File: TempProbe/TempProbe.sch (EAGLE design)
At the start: 15 parts, among them U2 ATTINY841

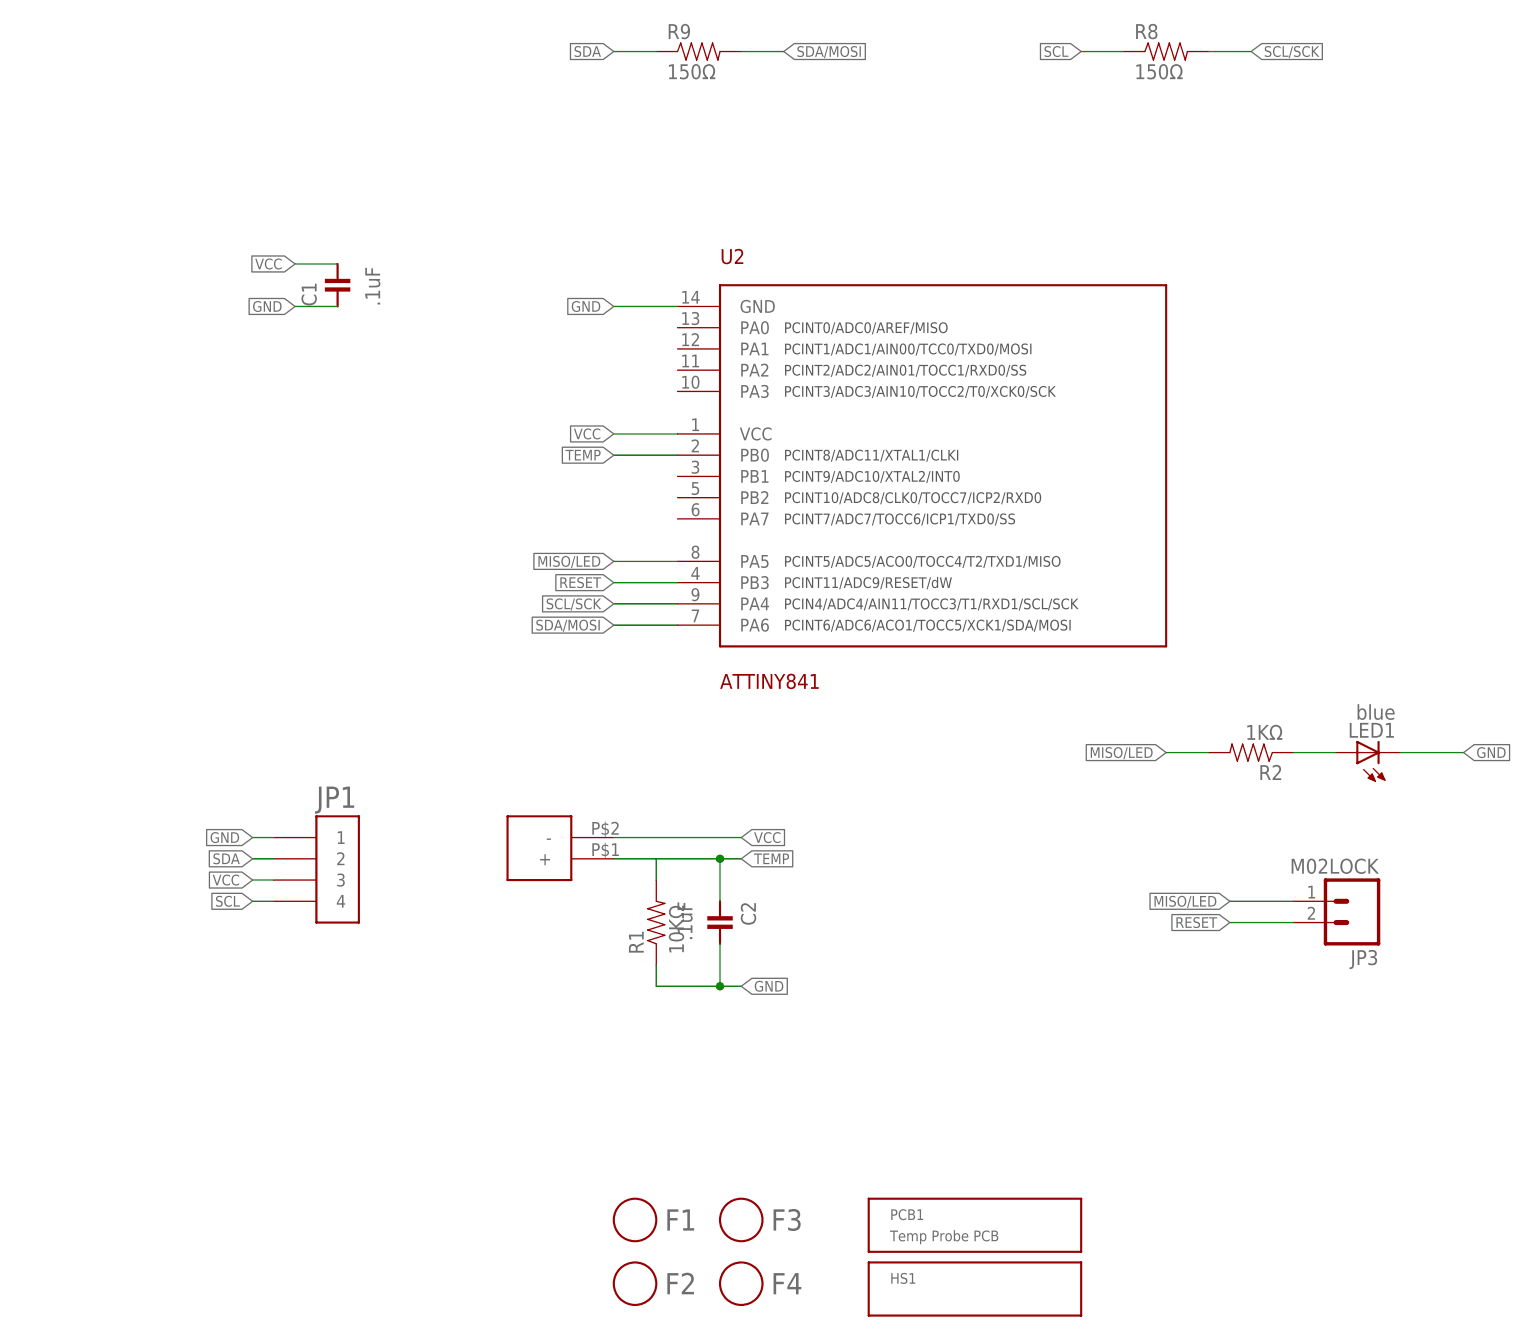
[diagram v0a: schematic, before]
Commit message: Changed to use Grove connector
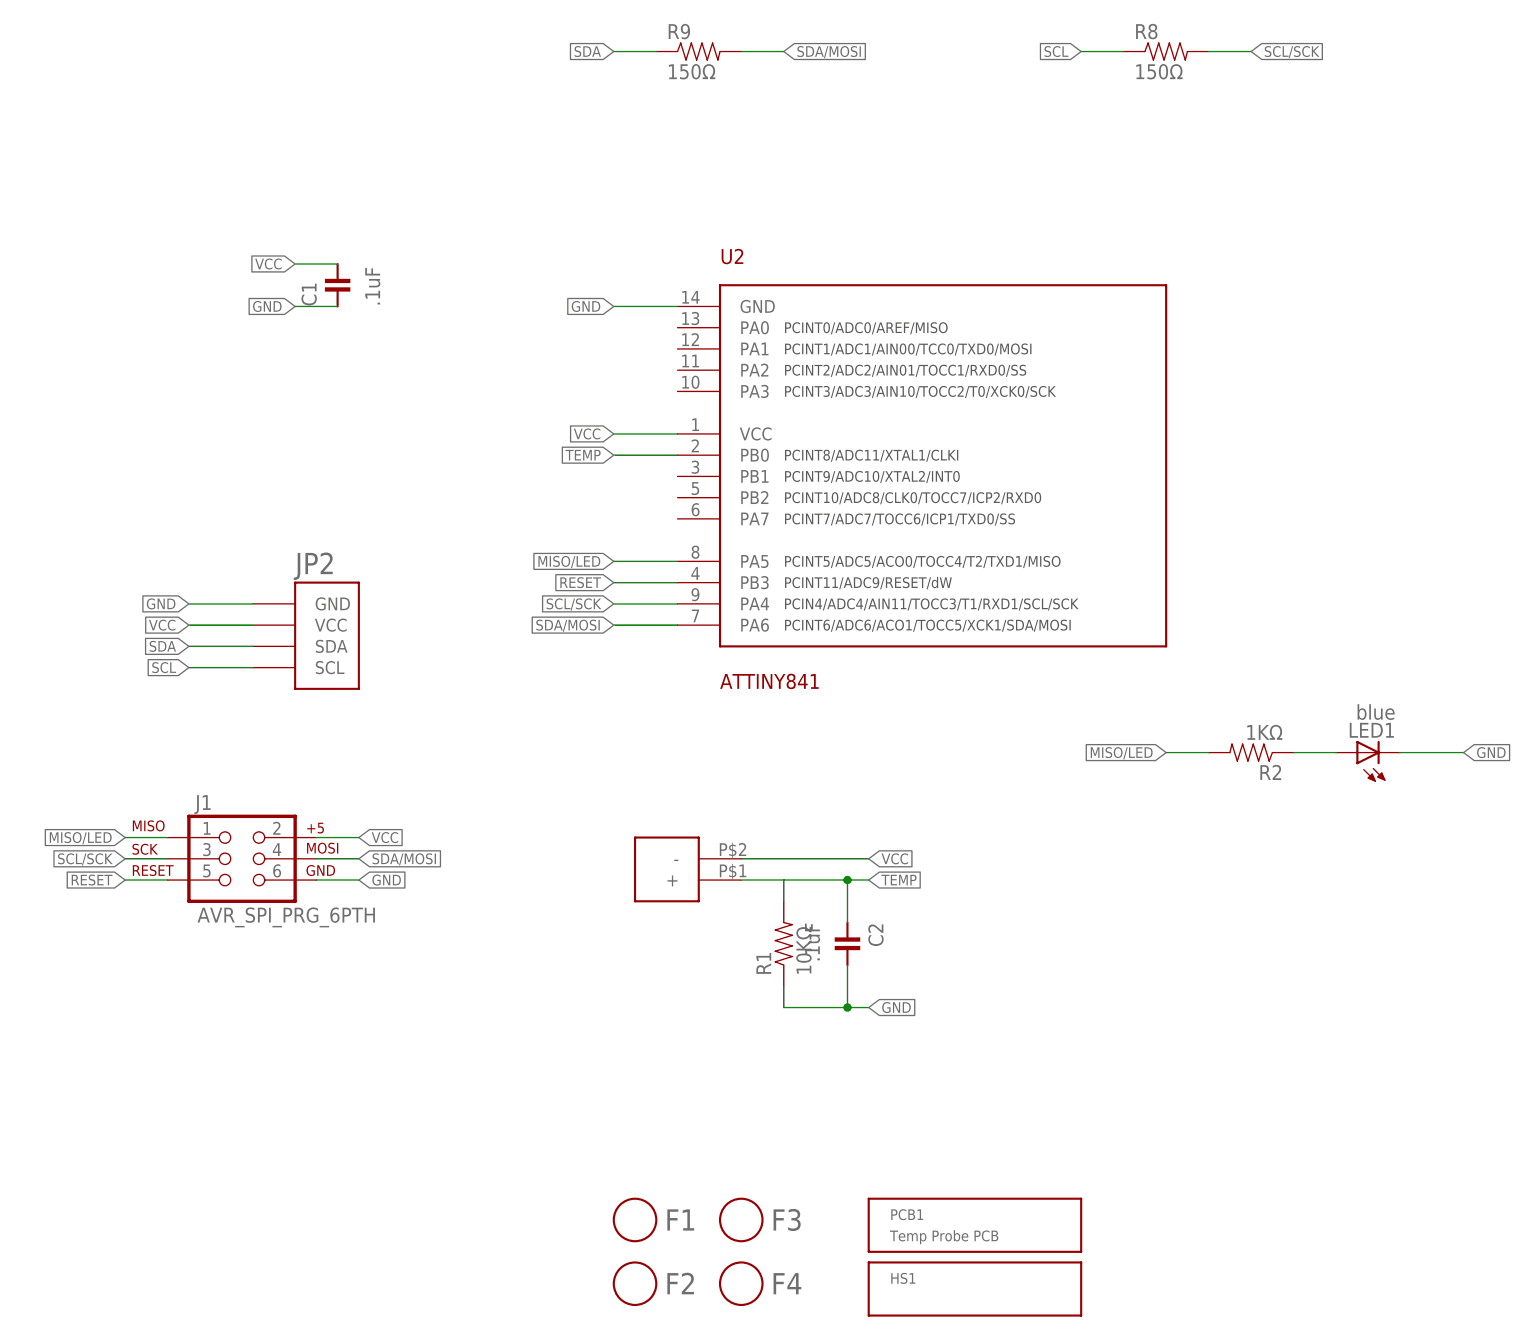
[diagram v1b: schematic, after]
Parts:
- removed JP1: HEADER-1X4-JST-PA-SIDE-SMD, Modulo:HEADER-1X4-JST-PA-SIDE-SMD
- removed JP3: M02LOCK, SparkFun-Connectors:M02LOCK
- added J1: AVR_SPI_PRG_6PTH, SparkFun-Connectors:AVR_SPI_PRG_6PTH
- added JP2: HEADER-MODULO, Modulo:HEADER-MODULO
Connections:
- net GND: now also J1.6, JP2.GND; no longer JP1.1
- net MISO/LED: now also J1.1; no longer JP3.1
- net RESET: now also J1.5; no longer JP3.2
- net SCL: now also JP2.SCL; no longer JP1.4
- net SCL/SCK: now also J1.3
- net SDA: now also JP2.SDA; no longer JP1.2
- net SDA/MOSI: now also J1.4
- net VCC: now also J1.2, JP2.VCC; no longer JP1.3
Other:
- moved on the sheet: C2, R1
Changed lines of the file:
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@@
 <part name="LED1" library="Modulo" deviceset="LED" device="-0805-BLUE" value="blue"/>
 <part name="R2" library="Modulo" deviceset="RESISTOR" device="-1KΩ" value="1KΩ"/>
-<part name="JP3" library="SparkFun-Connectors" deviceset="M02" device="LOCK">
-<attribute name="PARTNUM" value="EXCLUDE"/>
-</part>
 <part name="FRAME1" library="frames" deviceset="LETTER_L" device="">
 <attribute name="BOM" value="EXCLUDE"/>
@@
 <attribute name="PARTNUM" value="F221B1/2 CL210"/>
 </part>
-<part name="JP1" library="Modulo" deviceset="HEADER-1X4" device="-JST-PA-SIDE-SMD" value="HEADER-1X4-JST-PA-SIDE-SMD"/>
 <part name="U2" library="Modulo" deviceset="ATTINY841" device="" value="ATTINY841"/>
 <part name="R8" library="Modulo" deviceset="RESISTOR" device="-150Ω" value="150Ω">
@@
 <attribute name="PARTNUM" value="NTCLE413E2103F102L"/>
 </part>
+<part name="JP2" library="Modulo" deviceset="HEADER-MODULO" device=""/>
+<part name="J1" library="SparkFun-Connectors" deviceset="AVR_SPI_PRG_6" device="PTH"/>
 </parts>
 <sheets>
@@
 </plain>
 <instances>
-<instance part="C2" gate="G$1" x="93.98" y="68.58" rot="R180"/>
-<instance part="R1" gate="G$1" x="86.36" y="68.58" rot="R90"/>
+<instance part="C2" gate="G$1" x="109.22" y="66.04" rot="R180"/>
+<instance part="R1" gate="G$1" x="101.6" y="66.04" rot="R90"/>
 <instance part="C1" gate="G$1" x="48.26" y="144.78"/>
 <instance part="LED1" gate="G$1" x="170.18" y="88.9" rot="R90"/>
 <instance part="R2" gate="G$1" x="157.48" y="88.9" rot="R180"/>
-<instance part="JP3" gate="G$1" x="170.18" y="71.12" rot="R180">
-<attribute name="PARTNUM" x="170.18" y="71.12" size="1.27" layer="96" rot="R180" display="off"/>
-</instance>
 <instance part="FRAME1" gate="G$1" x="0" y="0">
 <attribute name="BOM" x="0" y="0" size="1.27" layer="96" display="off"/>
@@
 <attribute name="PARTNUM" x="116.84" y="22.86" size="1.27" layer="96" display="off"/>
 </instance>
-<instance part="JP1" gate="G$1" x="45.72" y="76.2"/>
 <instance part="U2" gate="G$1" x="99.06" y="114.3"/>
 <instance part="R8" gate="G$1" x="147.32" y="172.72">
@@
 <instance part="F3" gate="G$1" x="96.52" y="33.02"/>
 <instance part="F4" gate="G$1" x="96.52" y="25.4"/>
-<instance part="PROBE1" gate="G$1" x="73.66" y="76.2" rot="R180">
-<attribute name="PARTNUM" x="73.66" y="76.2" size="1.778" layer="96" rot="R180" display="off"/>
-</instance>
+<instance part="PROBE1" gate="G$1" x="88.9" y="73.66" rot="R180">
+<attribute name="PARTNUM" x="88.9" y="73.66" size="1.778" layer="96" rot="R180" display="off"/>
+</instance>
+<instance part="JP2" gate="G$1" x="45.72" y="101.6"/>
+<instance part="J1" gate="G$1" x="35.56" y="76.2"/>
 </instances>
 <busses>
@@
 <segment>
 <pinref part="R1" gate="G$1" pin="1"/>
-<wire x1="86.36" y1="63.5" x2="86.36" y2="60.96" width="0.1524" layer="91"/>
+<wire x1="101.6" y1="60.96" x2="101.6" y2="58.42" width="0.1524" layer="91"/>
 <pinref part="C2" gate="G$1" pin="1"/>
-<wire x1="93.98" y1="66.04" x2="93.98" y2="60.96" width="0.1524" layer="91"/>
-<wire x1="93.98" y1="60.96" x2="86.36" y2="60.96" width="0.1524" layer="91"/>
-<wire x1="93.98" y1="60.96" x2="96.52" y2="60.96" width="0.1524" layer="91"/>
-<label x="96.52" y="60.96" size="1.27" layer="95" xref="yes"/>
-<junction x="93.98" y="60.96"/>
+<wire x1="109.22" y1="63.5" x2="109.22" y2="58.42" width="0.1524" layer="91"/>
+<wire x1="109.22" y1="58.42" x2="101.6" y2="58.42" width="0.1524" layer="91"/>
+<wire x1="109.22" y1="58.42" x2="111.76" y2="58.42" width="0.1524" layer="91"/>
+<label x="111.76" y="58.42" size="1.27" layer="95" xref="yes"/>
+<junction x="109.22" y="58.42"/>
 </segment>
 <segment>
@@
 </segment>
 <segment>
-<pinref part="JP1" gate="G$1" pin="1"/>
-<wire x1="40.64" y1="78.74" x2="38.1" y2="78.74" width="0.1524" layer="91"/>
-<label x="38.1" y="78.74" size="1.27" layer="95" rot="R180" xref="yes"/>
-</segment>
-<segment>
 <pinref part="U2" gate="G$1" pin="GND"/>
 <wire x1="88.9" y1="142.24" x2="81.28" y2="142.24" width="0.1524" layer="91"/>
 <label x="81.28" y="142.24" size="1.27" layer="95" rot="MR0" xref="yes"/>
 </segment>
+<segment>
+<pinref part="JP2" gate="G$1" pin="GND"/>
+<wire x1="38.1" y1="106.68" x2="30.48" y2="106.68" width="0.1524" layer="91"/>
+<label x="30.48" y="106.68" size="1.27" layer="95" rot="R180" xref="yes"/>
+</segment>
+<segment>
+<pinref part="J1" gate="G$1" pin="6"/>
+<wire x1="45.72" y1="73.66" x2="50.8" y2="73.66" width="0.1524" layer="91"/>
+<label x="50.8" y="73.66" size="1.27" layer="95" xref="yes"/>
+</segment>
 </net>
 <net name="TEMP" class="0">
 <segment>
 <pinref part="R1" gate="G$1" pin="2"/>
-<wire x1="93.98" y1="76.2" x2="86.36" y2="76.2" width="0.1524" layer="91"/>
-<wire x1="86.36" y1="73.66" x2="86.36" y2="76.2" width="0.1524" layer="91"/>
+<wire x1="109.22" y1="73.66" x2="101.6" y2="73.66" width="0.1524" layer="91"/>
+<wire x1="101.6" y1="71.12" x2="101.6" y2="73.66" width="0.1524" layer="91"/>
 <pinref part="C2" gate="G$1" pin="2"/>
-<wire x1="93.98" y1="71.12" x2="93.98" y2="76.2" width="0.1524" layer="91"/>
-<wire x1="93.98" y1="76.2" x2="96.52" y2="76.2" width="0.1524" layer="91"/>
-<label x="96.52" y="76.2" size="1.27" layer="95" xref="yes"/>
-<junction x="93.98" y="76.2"/>
-<wire x1="81.28" y1="76.2" x2="86.36" y2="76.2" width="0.1524" layer="91"/>
+<wire x1="109.22" y1="68.58" x2="109.22" y2="73.66" width="0.1524" layer="91"/>
+<wire x1="109.22" y1="73.66" x2="111.76" y2="73.66" width="0.1524" layer="91"/>
+<label x="111.76" y="73.66" size="1.27" layer="95" xref="yes"/>
+<junction x="109.22" y="73.66"/>
+<wire x1="96.52" y1="73.66" x2="101.6" y2="73.66" width="0.1524" layer="91"/>
 <pinref part="PROBE1" gate="G$1" pin="+"/>
 </segment>
@@
 <net name="SDA" class="0">
 <segment>
-<pinref part="JP1" gate="G$1" pin="2"/>
-<wire x1="40.64" y1="76.2" x2="38.1" y2="76.2" width="0.1524" layer="91"/>
-<label x="38.1" y="76.2" size="1.27" layer="95" rot="R180" xref="yes"/>
-</segment>
-<segment>
 <pinref part="R9" gate="G$1" pin="1"/>
 <wire x1="86.36" y1="172.72" x2="81.28" y2="172.72" width="0.1524" layer="91"/>
 <label x="81.28" y="172.72" size="1.27" layer="95" rot="R180" xref="yes"/>
 </segment>
+<segment>
+<pinref part="JP2" gate="G$1" pin="SDA"/>
+<wire x1="38.1" y1="101.6" x2="30.48" y2="101.6" width="0.1524" layer="91"/>
+<label x="30.48" y="101.6" size="1.27" layer="95" rot="R180" xref="yes"/>
+</segment>
 </net>
 <net name="VCC" class="0">
@@
 </segment>
 <segment>
-<pinref part="JP1" gate="G$1" pin="3"/>
-<wire x1="40.64" y1="73.66" x2="38.1" y2="73.66" width="0.1524" layer="91"/>
-<label x="38.1" y="73.66" size="1.27" layer="95" rot="R180" xref="yes"/>
-</segment>
-<segment>
 <pinref part="U2" gate="G$1" pin="VCC"/>
 <wire x1="88.9" y1="127" x2="81.28" y2="127" width="0.1524" layer="91"/>
@@
 </segment>
 <segment>
-<wire x1="81.28" y1="78.74" x2="96.52" y2="78.74" width="0.1524" layer="91"/>
-<label x="96.52" y="78.74" size="1.27" layer="95" xref="yes"/>
+<wire x1="96.52" y1="76.2" x2="111.76" y2="76.2" width="0.1524" layer="91"/>
+<label x="111.76" y="76.2" size="1.27" layer="95" xref="yes"/>
 <pinref part="PROBE1" gate="G$1" pin="-"/>
 </segment>
+<segment>
+<pinref part="JP2" gate="G$1" pin="VCC"/>
+<wire x1="38.1" y1="104.14" x2="30.48" y2="104.14" width="0.1524" layer="91"/>
+<label x="30.48" y="104.14" size="1.27" layer="95" rot="R180" xref="yes"/>
+</segment>
+<segment>
+<pinref part="J1" gate="G$1" pin="2"/>
+<wire x1="45.72" y1="78.74" x2="50.8" y2="78.74" width="0.1524" layer="91"/>
+<label x="50.8" y="78.74" size="1.27" layer="95" xref="yes"/>
+</segment>
 </net>
 <net name="SCL" class="0">
-<segment>
-<pinref part="JP1" gate="G$1" pin="4"/>
-<wire x1="40.64" y1="71.12" x2="38.1" y2="71.12" width="0.1524" layer="91"/>
-<label x="38.1" y="71.12" size="1.27" layer="95" rot="R180" xref="yes"/>
-</segment>
 <segment>
 <pinref part="R8" gate="G$1" pin="1"/>
@@
 <label x="137.16" y="172.72" size="1.27" layer="95" rot="R180" xref="yes"/>
 </segment>
+<segment>
+<pinref part="JP2" gate="G$1" pin="SCL"/>
+<wire x1="38.1" y1="99.06" x2="30.48" y2="99.06" width="0.1524" layer="91"/>
+<label x="30.48" y="99.06" size="1.27" layer="95" rot="R180" xref="yes"/>
+</segment>
 </net>
 <net name="RESET" class="0">
@@
 </segment>
 <segment>
-<pinref part="JP3" gate="G$1" pin="2"/>
-<wire x1="162.56" y1="68.58" x2="154.94" y2="68.58" width="0.1524" layer="91"/>
-<label x="154.94" y="68.58" size="1.27" layer="95" rot="R180" xref="yes"/>
+<pinref part="J1" gate="G$1" pin="5"/>
+<wire x1="27.94" y1="73.66" x2="22.86" y2="73.66" width="0.1524" layer="91"/>
+<label x="22.86" y="73.66" size="1.27" layer="95" rot="R180" xref="yes"/>
 </segment>
 </net>
@@
 <label x="81.28" y="104.14" size="1.27" layer="95" rot="MR0" xref="yes"/>
 </segment>
+<segment>
+<pinref part="J1" gate="G$1" pin="4"/>
+<wire x1="45.72" y1="76.2" x2="50.8" y2="76.2" width="0.1524" layer="91"/>
+<label x="50.8" y="76.2" size="1.27" layer="95" xref="yes"/>
+</segment>
 </net>
 <net name="SCL/SCK" class="0">
@@
 <label x="81.28" y="106.68" size="1.27" layer="95" rot="MR0" xref="yes"/>
 </segment>
+<segment>
+<pinref part="J1" gate="G$1" pin="3"/>
+<wire x1="27.94" y1="76.2" x2="22.86" y2="76.2" width="0.1524" layer="91"/>
+<label x="22.86" y="76.2" size="1.27" layer="95" rot="R180" xref="yes"/>
+</segment>
 </net>
 <net name="MISO/LED" class="0">
@@
 </segment>
 <segment>
-<pinref part="JP3" gate="G$1" pin="1"/>
-<wire x1="162.56" y1="71.12" x2="154.94" y2="71.12" width="0.1524" layer="91"/>
-<label x="154.94" y="71.12" size="1.27" layer="95" rot="R180" xref="yes"/>
-</segment>
-<segment>
 <pinref part="R2" gate="G$1" pin="2"/>
 <wire x1="152.4" y1="88.9" x2="147.32" y2="88.9" width="0.1524" layer="91"/>
 <label x="147.32" y="88.9" size="1.27" layer="95" rot="R180" xref="yes"/>
 </segment>
-</net>
+<segment>
+<pinref part="J1" gate="G$1" pin="1"/>
+<wire x1="27.94" y1="78.74" x2="22.86" y2="78.74" width="0.1524" layer="91"/>
+<label x="22.86" y="78.74" size="1.27" layer="95" rot="R180" xref="yes"/>
+</segment>
+</net>
